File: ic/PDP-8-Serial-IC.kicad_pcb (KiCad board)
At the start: 2 copper layers, 125.7 x 62.2 mm, 61 parts, among them J1 Screw_Terminal_01x06, J2 DE9_Socket_MountingHoles, J3 FlipChip_01x18, Q1 2N3904, Q2 2N3904, Q3 2N3906, U1 MAX232, U2 74HCT14, U3 L78L05_TO92

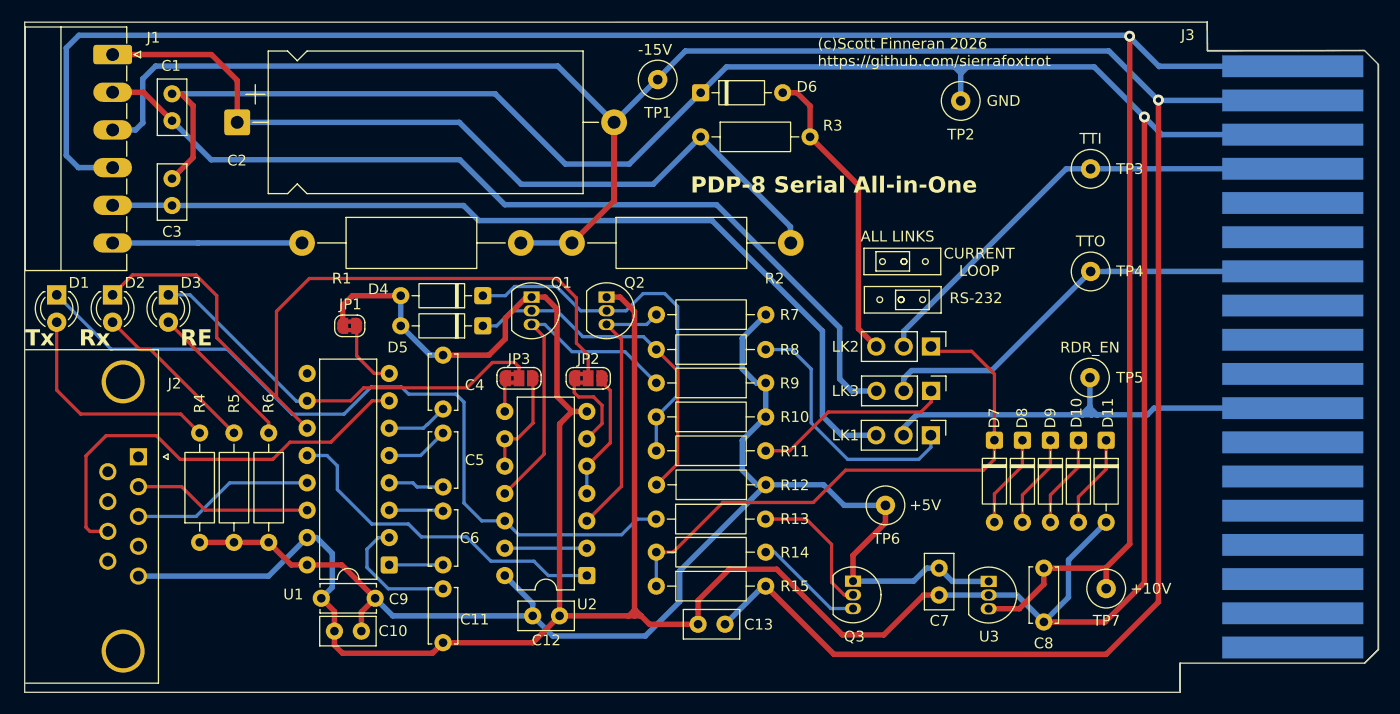
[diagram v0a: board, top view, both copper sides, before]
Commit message: Added improved flip-chip footprint and shared lib for IC variant
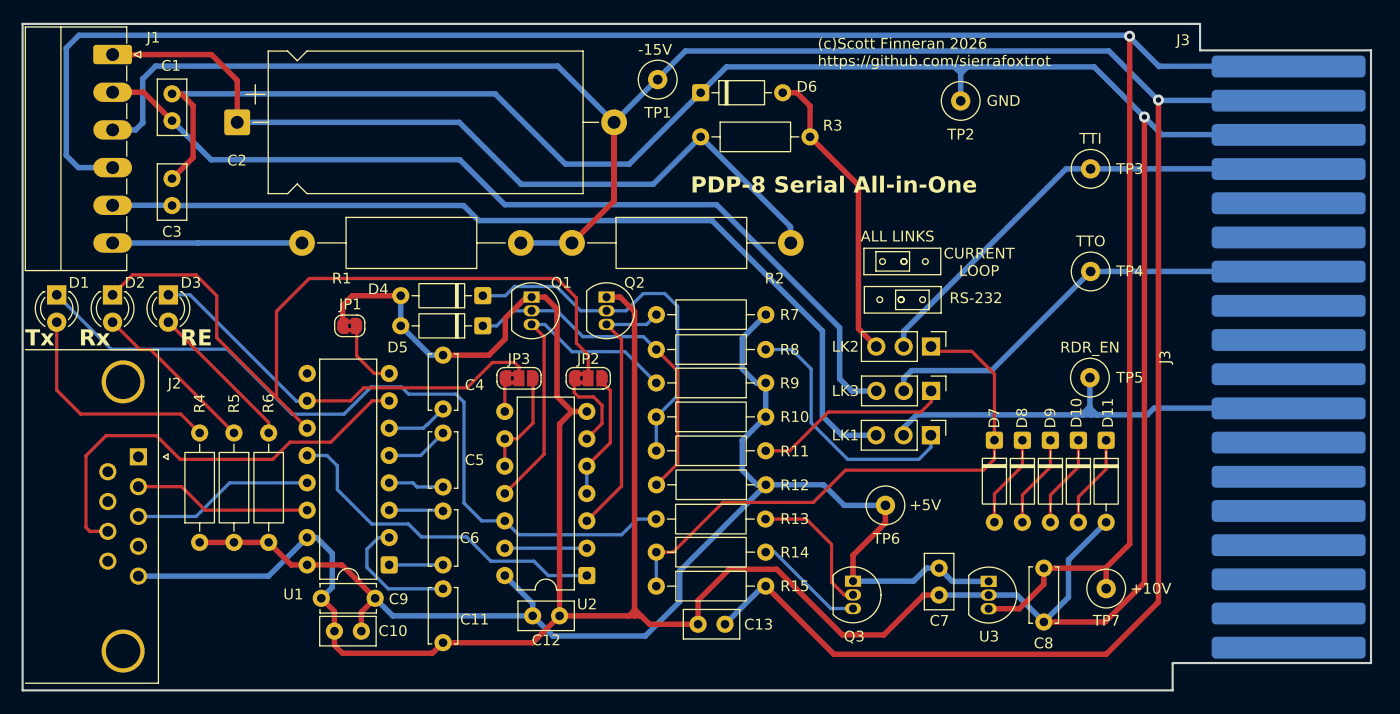
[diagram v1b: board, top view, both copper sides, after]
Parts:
- J3: footprint DEC:FlipChip_SingleSided_CardEdge -> DEC:DEC_single_short_holeless
- moved J3 2.54 mm to (213.8, 131.3), turned to 90 degrees
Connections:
- net /<NO NET> renamed /DSR
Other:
- board size 125.7 x 62.2 mm -> 125.2 x 61.9 mm
